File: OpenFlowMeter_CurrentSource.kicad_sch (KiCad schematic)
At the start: 21 parts, among them J2 Screw_Terminal_01x02, Q2 BC856, U6 LT1492

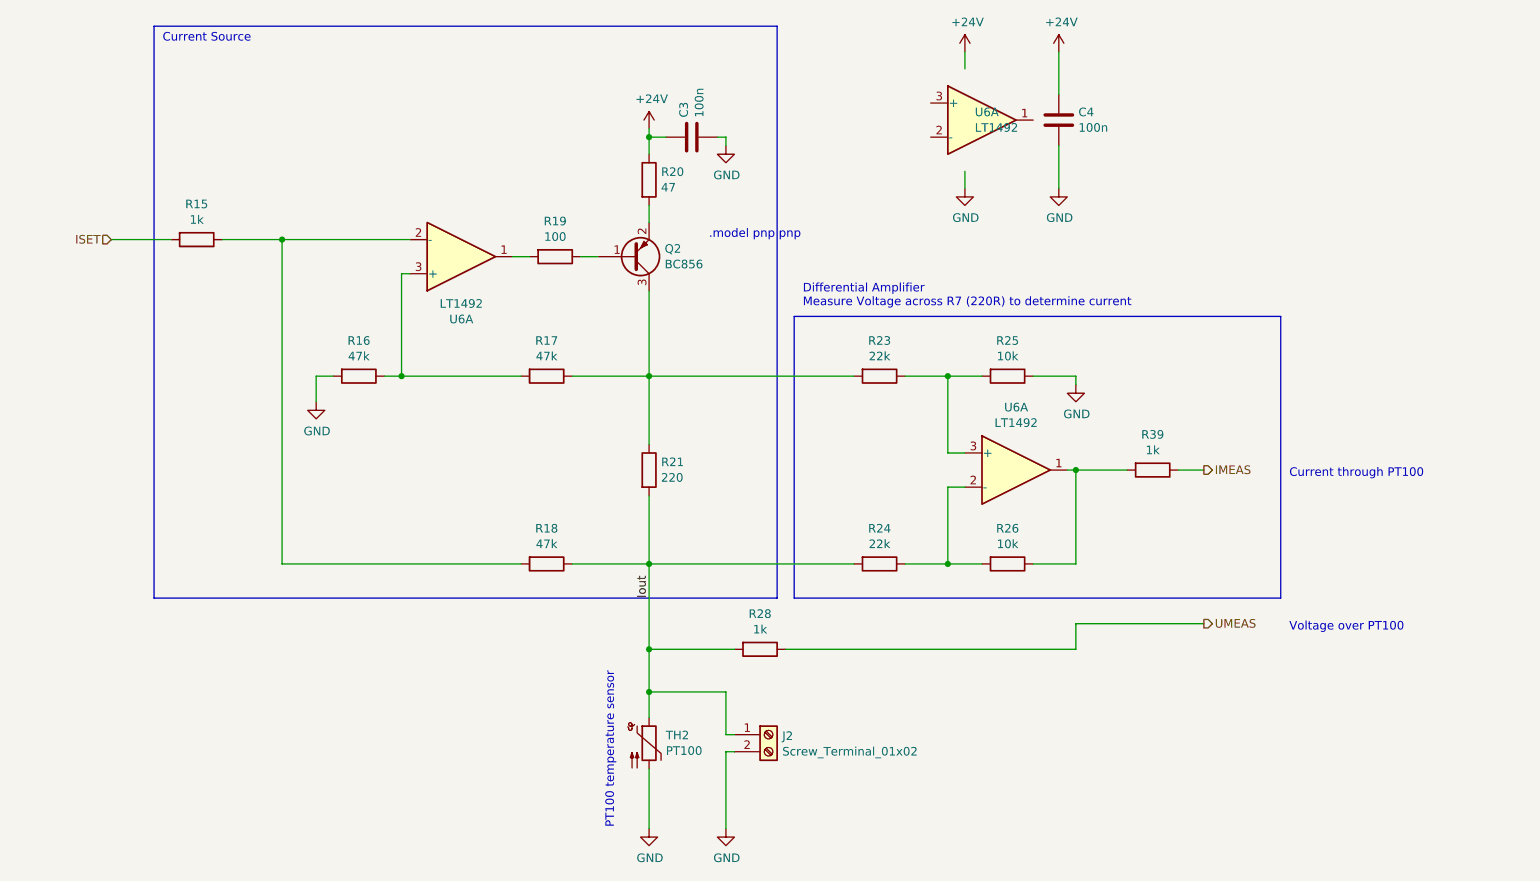
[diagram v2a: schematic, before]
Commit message: added write protection to EEPROM
added jumper, which can be opened and then the EEPROM is write protected.
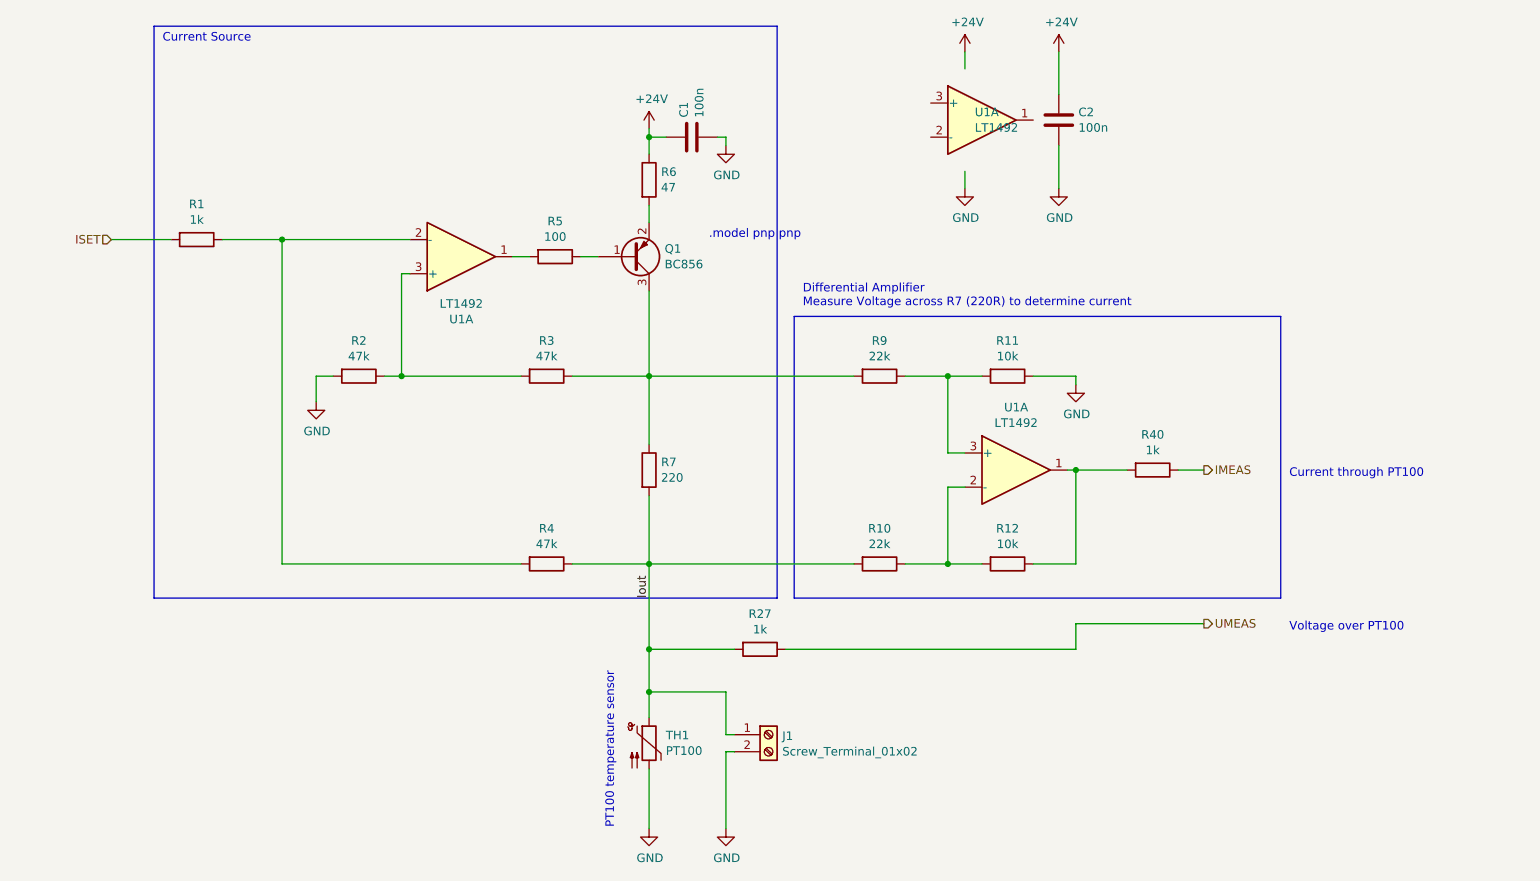
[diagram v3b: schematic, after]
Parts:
- renumbered C3 to C1, C4 to C2, J2 to J1, Q2 to Q1, R15 to R1, R24 to R10, R25 to R11, R26 to R12, R16 to R2, R28 to R27, R17 to R3, R18 to R4, R39 to R40, R19 to R5, R20 to R6, R21 to R7, R23 to R9, TH2 to TH1, U6 to U1
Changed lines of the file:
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@@
   (symbol (lib_id "Amplifier_Operational:LT1492") (at 90.17 83.82 0) (mirror x)
     (in_bom yes) (on_board yes)
-    (property "Reference" "U6" (id 0) (at 90.17 93.1418 0))
+    (property "Reference" "U1" (id 0) (at 90.17 93.1418 0))
     (property "Value" "LT1492" (id 1) (at 90.17 90.8304 0))
     (property "Footprint" "Package_SO:SOIC-8_3.9x4.9mm_P1.27mm" (id 2) (at 90.17 83.82 0)
@@
   (symbol (lib_id "Amplifier_Operational:LT1492") (at 172.72 115.57 0)
     (in_bom yes) (on_board yes)
-    (property "Reference" "U6" (id 0) (at 172.72 106.2482 0))
+    (property "Reference" "U1" (id 0) (at 172.72 106.2482 0))
     (property "Value" "LT1492" (id 1) (at 172.72 108.5596 0))
     (property "Footprint" "Package_SO:SOIC-8_3.9x4.9mm_P1.27mm" (id 2) (at 172.72 115.57 0)
@@
   (symbol (lib_id "Amplifier_Operational:LT1492") (at 167.64 63.5 0)
     (in_bom yes) (on_board yes)
-    (property "Reference" "U6" (id 0) (at 166.5732 62.3316 0)
+    (property "Reference" "U1" (id 0) (at 166.5732 62.3316 0)
       (effects (font (size 1.27 1.27)) (justify left))
     )
@@
   (symbol (lib_id "Device:R") (at 50.8 81.28 270)
     (in_bom yes) (on_board yes)
-    (property "Reference" "R15" (id 0) (at 50.8 76.0222 90))
+    (property "Reference" "R1" (id 0) (at 50.8 76.0222 90))
     (property "Value" "1k" (id 1) (at 50.8 78.3336 90))
     (property "Footprint" "Resistor_SMD:R_0603_1608Metric" (id 2) (at 50.8 79.502 90)
@@
   (symbol (lib_id "Device:R") (at 102.87 129.54 270)
     (in_bom yes) (on_board yes)
-    (property "Reference" "R18" (id 0) (at 102.87 124.2822 90))
+    (property "Reference" "R4" (id 0) (at 102.87 124.2822 90))
     (property "Value" "47k" (id 1) (at 102.87 126.5936 90))
     (property "Footprint" "Resistor_SMD:R_0603_1608Metric" (id 2) (at 102.87 127.762 90)
@@
   (symbol (lib_id "Device:R") (at 118.11 72.39 0)
     (in_bom yes) (on_board yes)
-    (property "Reference" "R20" (id 0) (at 119.888 71.2216 0)
+    (property "Reference" "R6" (id 0) (at 119.888 71.2216 0)
       (effects (font (size 1.27 1.27)) (justify left))
     )
@@
   (symbol (lib_id "Device:R") (at 104.14 83.82 270)
     (in_bom yes) (on_board yes)
-    (property "Reference" "R19" (id 0) (at 104.14 78.5622 90))
+    (property "Reference" "R5" (id 0) (at 104.14 78.5622 90))
     (property "Value" "100" (id 1) (at 104.14 80.8736 90))
     (property "Footprint" "Resistor_SMD:R_0603_1608Metric" (id 2) (at 104.14 82.042 90)
@@
   (symbol (lib_id "Device:R") (at 118.11 115.57 0)
     (in_bom yes) (on_board yes)
-    (property "Reference" "R21" (id 0) (at 119.888 114.4016 0)
+    (property "Reference" "R7" (id 0) (at 119.888 114.4016 0)
       (effects (font (size 1.27 1.27)) (justify left))
     )
@@
   (symbol (lib_id "Device:R") (at 102.87 101.6 270)
     (in_bom yes) (on_board yes)
-    (property "Reference" "R17" (id 0) (at 102.87 96.3422 90))
+    (property "Reference" "R3" (id 0) (at 102.87 96.3422 90))
     (property "Value" "47k" (id 1) (at 102.87 98.6536 90))
     (property "Footprint" "Resistor_SMD:R_0603_1608Metric" (id 2) (at 102.87 99.822 90)
@@
   (symbol (lib_id "Device:R") (at 74.93 101.6 270)
     (in_bom yes) (on_board yes)
-    (property "Reference" "R16" (id 0) (at 74.93 96.3422 90))
+    (property "Reference" "R2" (id 0) (at 74.93 96.3422 90))
     (property "Value" "47k" (id 1) (at 74.93 98.6536 90))
     (property "Footprint" "Resistor_SMD:R_0603_1608Metric" (id 2) (at 74.93 99.822 90)
@@
   (symbol (lib_id "power:GND") (at 68.58 105.41 0)
     (in_bom yes) (on_board yes)
-    (property "Reference" "#PWR0101" (id 0) (at 68.58 111.76 0)
+    (property "Reference" "#PWR02" (id 0) (at 68.58 111.76 0)
       (effects (font (size 1.27 1.27)) hide)
     )
@@
   (symbol (lib_id "power:+24V") (at 118.11 64.77 0)
     (in_bom yes) (on_board yes)
-    (property "Reference" "#PWR0103" (id 0) (at 118.11 68.58 0)
+    (property "Reference" "#PWR03" (id 0) (at 118.11 68.58 0)
       (effects (font (size 1.27 1.27)) hide)
     )
@@
   (symbol (lib_id "power:+24V") (at 165.1 53.34 0)
     (in_bom yes) (on_board yes)
-    (property "Reference" "#PWR0104" (id 0) (at 165.1 57.15 0)
+    (property "Reference" "#PWR05" (id 0) (at 165.1 57.15 0)
       (effects (font (size 1.27 1.27)) hide)
     )
@@
   (symbol (lib_id "power:GND") (at 165.1 73.66 0)
     (in_bom yes) (on_board yes)
-    (property "Reference" "#PWR0105" (id 0) (at 165.1 80.01 0)
+    (property "Reference" "#PWR06" (id 0) (at 165.1 80.01 0)
       (effects (font (size 1.27 1.27)) hide)
     )
@@
   (symbol (lib_id "Device:R") (at 152.4 101.6 270)
     (in_bom yes) (on_board yes)
-    (property "Reference" "R23" (id 0) (at 152.4 96.3422 90))
+    (property "Reference" "R9" (id 0) (at 152.4 96.3422 90))
     (property "Value" "22k" (id 1) (at 152.4 98.6536 90))
     (property "Footprint" "Resistor_SMD:R_0603_1608Metric" (id 2) (at 152.4 99.822 90)
@@
   (symbol (lib_id "Device:R") (at 152.4 129.54 270)
     (in_bom yes) (on_board yes)
-    (property "Reference" "R24" (id 0) (at 152.4 124.2822 90))
+    (property "Reference" "R10" (id 0) (at 152.4 124.2822 90))
     (property "Value" "22k" (id 1) (at 152.4 126.5936 90))
     (property "Footprint" "Resistor_SMD:R_0603_1608Metric" (id 2) (at 152.4 127.762 90)
@@
   (symbol (lib_id "Device:R") (at 171.45 101.6 270)
     (in_bom yes) (on_board yes)
-    (property "Reference" "R25" (id 0) (at 171.45 96.3422 90))
+    (property "Reference" "R11" (id 0) (at 171.45 96.3422 90))
     (property "Value" "10k" (id 1) (at 171.45 98.6536 90))
     (property "Footprint" "Resistor_SMD:R_0603_1608Metric" (id 2) (at 171.45 99.822 90)
@@
   (symbol (lib_id "Device:R") (at 171.45 129.54 270)
     (in_bom yes) (on_board yes)
-    (property "Reference" "R26" (id 0) (at 171.45 124.2822 90))
+    (property "Reference" "R12" (id 0) (at 171.45 124.2822 90))
     (property "Value" "10k" (id 1) (at 171.45 126.5936 90))
     (property "Footprint" "Resistor_SMD:R_0603_1608Metric" (id 2) (at 171.45 127.762 90)
@@
   (symbol (lib_id "power:GND") (at 181.61 102.87 0)
     (in_bom yes) (on_board yes)
-    (property "Reference" "#PWR0106" (id 0) (at 181.61 109.22 0)
+    (property "Reference" "#PWR07" (id 0) (at 181.61 109.22 0)
       (effects (font (size 1.27 1.27)) hide)
     )
@@
   (symbol (lib_id "power:GND") (at 118.11 168.91 0)
     (in_bom yes) (on_board yes)
-    (property "Reference" "#PWR0107" (id 0) (at 118.11 175.26 0)
+    (property "Reference" "#PWR04" (id 0) (at 118.11 175.26 0)
       (effects (font (size 1.27 1.27)) hide)
     )
@@
   (symbol (lib_id "Transistor_BJT:BC856") (at 115.57 83.82 0) (mirror x)
     (in_bom yes) (on_board yes)
-    (property "Reference" "Q2" (id 0) (at 120.4214 82.6516 0)
+    (property "Reference" "Q1" (id 0) (at 120.4214 82.6516 0)
       (effects (font (size 1.27 1.27)) (justify left))
     )
@@
   (symbol (lib_id "Connector:Screw_Terminal_01x02") (at 135.89 154.94 0)
     (in_bom yes) (on_board yes)
-    (property "Reference" "J2" (id 0) (at 137.922 155.1432 0)
+    (property "Reference" "J1" (id 0) (at 137.922 155.1432 0)
       (effects (font (size 1.27 1.27)) (justify left))
     )
@@
   (symbol (lib_id "power:GND") (at 129.54 168.91 0)
     (in_bom yes) (on_board yes)
-    (property "Reference" "#PWR0111" (id 0) (at 129.54 175.26 0)
+    (property "Reference" "#PWR0110" (id 0) (at 129.54 175.26 0)
       (effects (font (size 1.27 1.27)) hide)
     )
@@
   (symbol (lib_id "Device:R") (at 134.62 142.24 270)
     (in_bom yes) (on_board yes)
-    (property "Reference" "R28" (id 0) (at 134.62 136.9822 90))
+    (property "Reference" "R27" (id 0) (at 134.62 136.9822 90))
     (property "Value" "1k" (id 1) (at 134.62 139.2936 90))
     (property "Footprint" "Resistor_SMD:R_0603_1608Metric" (id 2) (at 134.62 140.462 90)
@@
   (symbol (lib_id "Sensor_Temperature:PT100") (at 118.11 156.21 0)
     (in_bom yes) (on_board yes)
-    (property "Reference" "TH2" (id 0) (at 120.5992 155.0416 0)
+    (property "Reference" "TH1" (id 0) (at 120.5992 155.0416 0)
       (effects (font (size 1.27 1.27)) (justify left))
     )
@@
   (symbol (lib_id "Device:C") (at 179.07 63.5 0)
     (in_bom yes) (on_board yes)
-    (property "Reference" "C4" (id 0) (at 181.991 62.3316 0)
+    (property "Reference" "C2" (id 0) (at 181.991 62.3316 0)
       (effects (font (size 1.27 1.27)) (justify left))
     )
@@
   (symbol (lib_id "Device:C") (at 124.46 66.04 90)
     (in_bom yes) (on_board yes)
-    (property "Reference" "C3" (id 0) (at 123.2916 63.119 0)
+    (property "Reference" "C1" (id 0) (at 123.2916 63.119 0)
       (effects (font (size 1.27 1.27)) (justify left))
     )
@@
   (symbol (lib_id "power:GND") (at 129.54 67.31 0)
     (in_bom yes) (on_board yes)
-    (property "Reference" "#PWR014" (id 0) (at 129.54 73.66 0)
+    (property "Reference" "#PWR011" (id 0) (at 129.54 73.66 0)
       (effects (font (size 1.27 1.27)) hide)
     )
@@
   (symbol (lib_id "power:GND") (at 179.07 73.66 0)
     (in_bom yes) (on_board yes)
-    (property "Reference" "#PWR016" (id 0) (at 179.07 80.01 0)
+    (property "Reference" "#PWR013" (id 0) (at 179.07 80.01 0)
       (effects (font (size 1.27 1.27)) hide)
     )
@@
   (symbol (lib_id "power:+24V") (at 179.07 53.34 0)
     (in_bom yes) (on_board yes)
-    (property "Reference" "#PWR015" (id 0) (at 179.07 57.15 0)
+    (property "Reference" "#PWR012" (id 0) (at 179.07 57.15 0)
       (effects (font (size 1.27 1.27)) hide)
     )
@@
   (symbol (lib_id "Device:R") (at 193.04 115.57 270)
     (in_bom yes) (on_board yes)
-    (property "Reference" "R39" (id 0) (at 193.04 110.3122 90))
+    (property "Reference" "R40" (id 0) (at 193.04 110.3122 90))
     (property "Value" "1k" (id 1) (at 193.04 112.6236 90))
     (property "Footprint" "Resistor_SMD:R_0603_1608Metric" (id 2) (at 193.04 113.792 90)

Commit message: Some minor cleanups
Removed DRCs and did some minor cleanups.
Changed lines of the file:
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@@
     (stroke (width 0) (type default) (color 0 0 0 0))
   )
-  (wire (pts (xy 38.1 81.28) (xy 46.99 81.28))
+  (wire (pts (xy 30.48 81.28) (xy 46.99 81.28))
     (stroke (width 0) (type default) (color 0 0 0 0))
   )
@@
     (effects (font (size 1.27 1.27)) (justify left bottom))
   )
-  (hierarchical_label "ISET" (shape input) (at 38.1 81.28 180)
+  (hierarchical_label "ISET" (shape input) (at 30.48 81.28 180)
     (effects (font (size 1.27 1.27)) (justify right))
   )
